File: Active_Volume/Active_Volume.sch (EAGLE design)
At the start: 10 parts, among them U1 XR_PREAMP

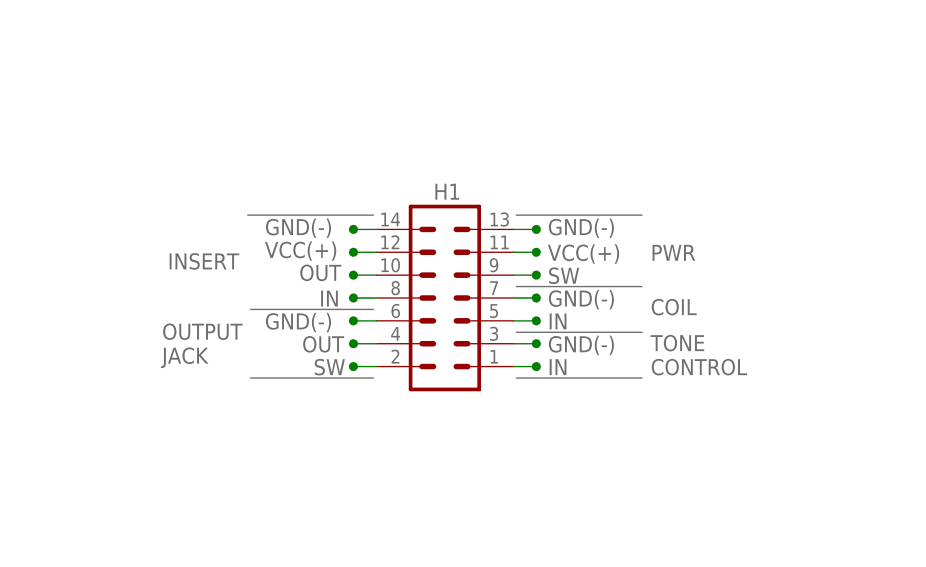
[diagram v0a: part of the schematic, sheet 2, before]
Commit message: Updates/ label modifications to make them consistent
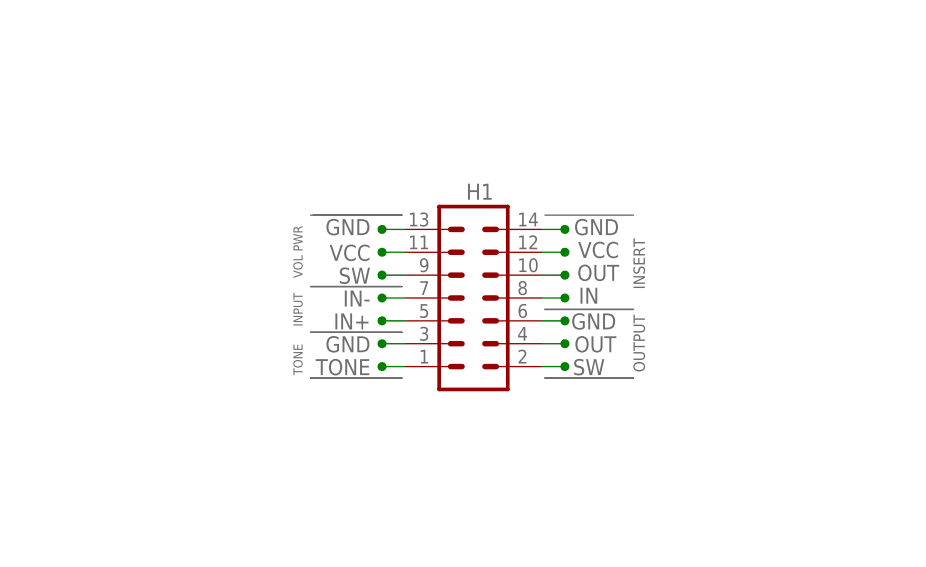
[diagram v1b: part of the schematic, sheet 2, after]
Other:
- note added: "GND"
- note added: "IN+"
- note added: "IN-"
- note added: "INPUT"
- note added: "OUTPUT"
- note added: "TONE"
- note added: "VCC"
- note added: "VOL PWR"
- note removed: "-(SW)"
- note removed: "COIL"
- note removed: "GND(-)"
- note removed: "OUTPUT JACK"
- note removed: "PWR"
- note removed: "TONE CONTROL"
- note removed: "VCC(+)"
- moved on the sheet: H1

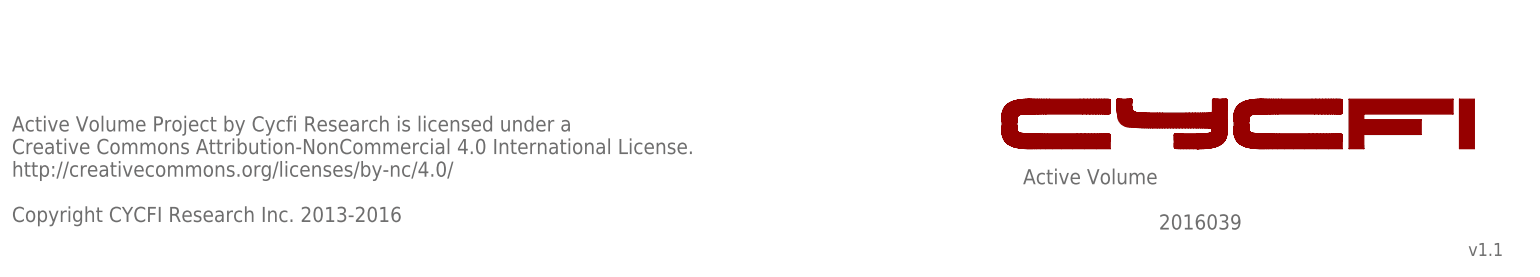
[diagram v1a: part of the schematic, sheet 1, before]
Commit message: Updated schematic licenses
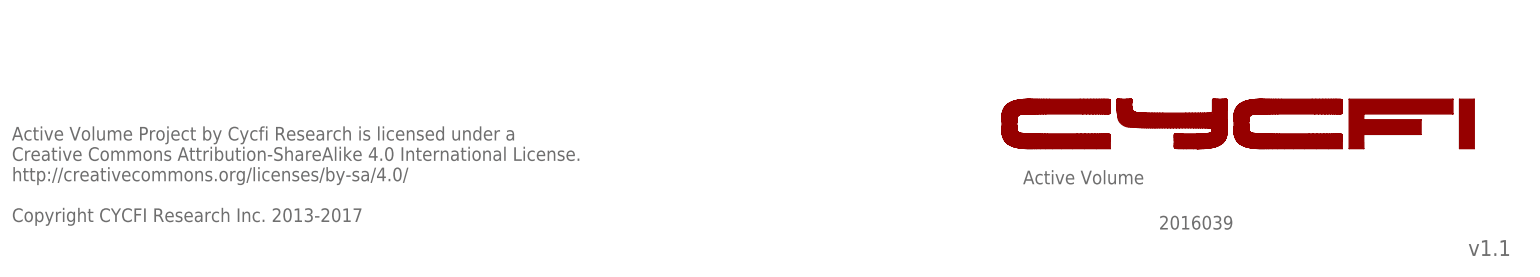
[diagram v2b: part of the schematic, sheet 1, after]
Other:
- note added: "Active Volume Project by Cycfi Research is licensed under a Creative Commons Attribution-ShareAlike 4.0 International License. http://creativecommons.org/licenses/by-sa/4.0/ Copyright CYCFI Research Inc. 2013-2017"
- note removed: "Active Volume Project by Cycfi Research is licensed under a Creative Commons Attribution-NonCommercial 4.0 International License. http://creativecommons.org/licenses/by-nc/4.0/ Copyright CYCFI Research Inc. 2013-2016"
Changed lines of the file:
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@@
 <setting verticaltext="up"/>
 </settings>
-<grid distance="0.0125" unitdist="inch" unit="inch" style="lines" multiple="1" display="yes" altdistance="0.01" altunitdist="inch" altunit="inch"/>
+<grid distance="0.1" unitdist="inch" unit="inch" style="lines" multiple="1" display="no" altdistance="0.01" altunitdist="inch" altunit="inch"/>
 <layers>
 <layer number="1" name="Top" color="4" fill="1" visible="no" active="no"/>
@@
 *POTENTIOMETER BREAKOUT = SMD pads
 for potentiometer breakout board (POT1)</text>
-<text x="177.8" y="19.05" size="2.54" layer="95">Active Volume</text>
-<text x="252.73" y="6.985" size="2.1844" layer="95">v1.1</text>
-<text x="7.62" y="12.7" size="2.54" layer="95">Active Volume Project by Cycfi Research is licensed under a
-Creative Commons Attribution-NonCommercial 4.0 International License.
-http://creativecommons.org/licenses/by-nc/4.0/
-Copyright CYCFI Research Inc. 2013-2016</text>
-<text x="200.66" y="11.43" size="2.54" layer="95">2016039</text>
+<text x="177.8" y="19.05" size="2.286" layer="95" font="vector">Active Volume</text>
+<text x="252.73" y="6.985" size="2.667" layer="95" font="vector">v1.1</text>
+<text x="7.62" y="12.7" size="2.286" layer="95" font="vector">Active Volume Project by Cycfi Research is licensed under a
+Creative Commons Attribution-ShareAlike 4.0 International License.
+http://creativecommons.org/licenses/by-sa/4.0/
+Copyright CYCFI Research Inc. 2013-2017</text>
+<text x="200.66" y="11.43" size="2.286" layer="95" font="vector">2016039</text>
 <wire x1="192.47528125" y1="25.047221875" x2="190.115640625" y2="25.047221875" width="0" layer="94"/>
 <wire x1="190.115640625" y1="25.047221875" x2="188.10833125" y2="25.047225" width="0" layer="94"/>
@@
 <instance part="FRAME1" gate="G$1" x="0" y="0"/>
 <instance part="FRAME1" gate="G$2" x="162.56" y="0" smashed="yes">
-<attribute name="LAST_DATE_TIME" x="175.26" y="1.27" size="2.54" layer="94" font="vector"/>
-<attribute name="SHEET" x="248.92" y="1.27" size="2.54" layer="94" font="vector"/>
+<attribute name="LAST_DATE_TIME" x="175.26" y="1.27" size="2.667" layer="94" font="vector"/>
+<attribute name="SHEET" x="248.92" y="1.27" size="2.667" layer="94" font="vector"/>
 </instance>
 </instances>
@@
 <text x="147.0025" y="106.68" size="1.778" layer="95" rot="MR0">IN</text>
 <text x="149.225" y="109.22" size="1.778" layer="95" rot="MR0">OUT</text>
-<text x="177.8" y="19.05" size="2.54" layer="95">Active Volume</text>
-<text x="252.73" y="6.985" size="2.1844" layer="95">v1.1</text>
-<text x="7.62" y="12.7" size="2.54" layer="95">Active Volume Project by Cycfi Research is licensed under a
-Creative Commons Attribution-NonCommercial 4.0 International License.
-http://creativecommons.org/licenses/by-nc/4.0/
-Copyright CYCFI Research Inc. 2013-2016</text>
-<text x="200.66" y="11.43" size="2.54" layer="95">2016039</text>
+<text x="177.8" y="19.05" size="2.667" layer="95" font="vector">Active Volume</text>
+<text x="252.73" y="6.985" size="2.667" layer="95" font="vector">v1.1</text>
+<text x="7.62" y="12.7" size="2.667" layer="95" font="vector">Active Volume Project by Cycfi Research is licensed under a
+Creative Commons Attribution-ShareAlike 4.0 International License.
+http://creativecommons.org/licenses/by-sa/4.0/
+Copyright CYCFI Research Inc. 2013-2017</text>
+<text x="200.66" y="11.43" size="2.667" layer="95" font="vector">2016039</text>
 <wire x1="192.47528125" y1="25.047221875" x2="190.115640625" y2="25.047221875" width="0" layer="94"/>
 <wire x1="190.115640625" y1="25.047221875" x2="188.10833125" y2="25.047225" width="0" layer="94"/>
@@
 <instance part="FRAME2" gate="G$1" x="0" y="0"/>
 <instance part="FRAME2" gate="G$2" x="162.56" y="0" smashed="yes">
-<attribute name="LAST_DATE_TIME" x="175.26" y="1.27" size="2.54" layer="94" font="vector"/>
-<attribute name="SHEET" x="248.92" y="1.27" size="2.54" layer="94" font="vector"/>
+<attribute name="LAST_DATE_TIME" x="175.26" y="1.27" size="2.667" layer="94" font="vector"/>
+<attribute name="SHEET" x="248.92" y="1.27" size="2.667" layer="94" font="vector"/>
 </instance>
 </instances>
